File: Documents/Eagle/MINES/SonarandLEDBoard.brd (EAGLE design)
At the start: 60.6 x 49.5 mm, 21 parts, among them X1 B2B-XH-2, X16 B2B-XH-2, X17 B2B-XH-2, X18 B2B-XH-2, X19 B2B-XH-2, X2 B2B-XH-2, X20 B2B-XH-2, X21 B2B-XH-2, X3 B4B-XH-2, X4 B4B-XH-2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

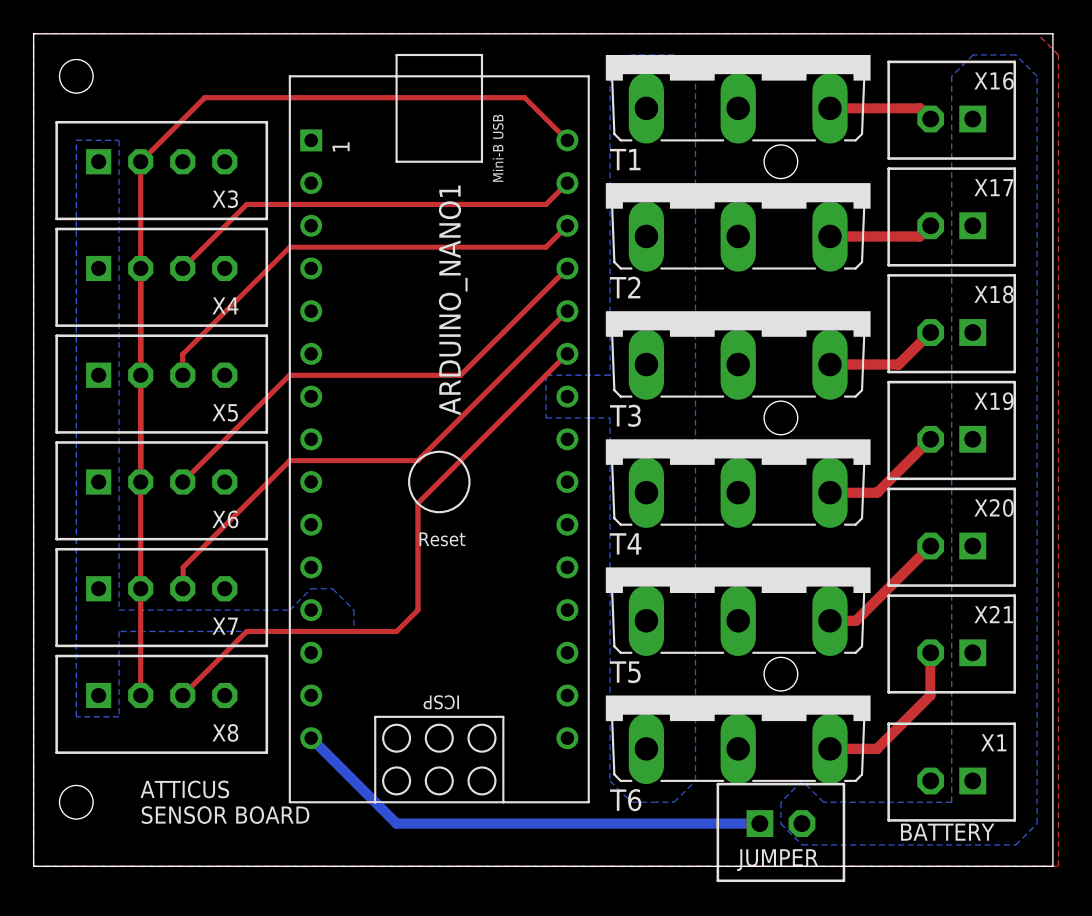
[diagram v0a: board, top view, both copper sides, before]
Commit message: Added 3-head breakouts to both boards and team name
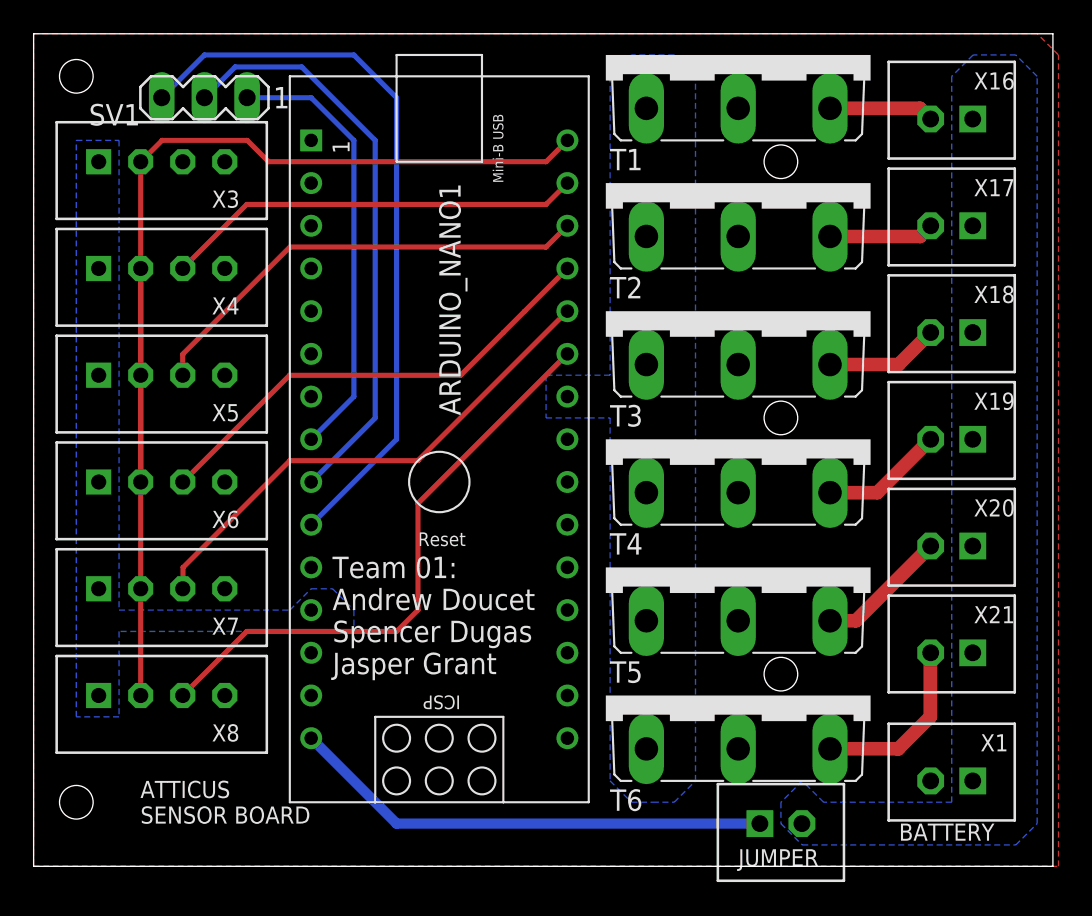
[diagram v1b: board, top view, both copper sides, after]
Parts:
- added SV1: (no value), con-lstb:MA03-1
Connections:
- new net N$1: ARDUINO_NANO1.8, SV1.1
- new net N$3: ARDUINO_NANO1.9, SV1.2
- new net N$4: ARDUINO_NANO1.10, SV1.3
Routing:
- net N$4: track 0.00 -> 43.6 mm
- net N$3: track 0.00 -> 34.6 mm
- net N$1: track 0.00 -> 26.2 mm
- net N$34: track 72.5 -> 71.4 mm
- net N$38: track 9.83 -> 10.6 mm
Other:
- board text added: "Team 01: Andrew Doucet Spencer Dugas Jasper Grant"
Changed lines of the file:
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@@
 <hole x="43.18" y="41.91" drill="2"/>
 <hole x="43.18" y="57.15" drill="2"/>
+<text x="16.51" y="41.91" size="1.27" layer="25">Team 01:
+Andrew Doucet
+Spencer Dugas
+Jasper Grant</text>
 </plain>
 <attributes>
@@
 </element>
 <element name="X2" library="con-JST XH" library_urn="urn:adsk.eagle:library:29976298" package="B2B-XH-A" package3d_urn="urn:adsk.eagle:package:29976402/1" value="B2B-XH-2" x="43.18" y="33.02" smashed="yes" rot="R180"/>
+<element name="SV1" library="con-lstb" library_urn="urn:adsk.eagle:library:162" package="MA03-1" package3d_urn="urn:adsk.eagle:package:8339/1" value="" x="8.89" y="76.2" smashed="yes" rot="R180">
+<attribute name="MF" value="" x="8.89" y="76.2" size="1.778" layer="27" rot="R180" display="off"/>
+<attribute name="MPN" value="" x="8.89" y="76.2" size="1.778" layer="27" rot="R180" display="off"/>
+<attribute name="NAME" x="5.08" y="75.819" size="1.27" layer="25" ratio="10" rot="R180"/>
+<attribute name="OC_FARNELL" value="unknown" x="8.89" y="76.2" size="1.778" layer="27" rot="R180" display="off"/>
+<attribute name="OC_NEWARK" value="unknown" x="8.89" y="76.2" size="1.778" layer="27" rot="R180" display="off"/>
+<attribute name="POPULARITY" value="48" x="8.89" y="76.2" size="1.778" layer="27" rot="R180" display="off"/>
+<attribute name="VALUE" x="12.7" y="79.121" size="1.27" layer="27" ratio="10" rot="R180"/>
+</element>
 </elements>
 <signals>
@@
 <wire x1="5.1" y1="59.69" x2="5.1" y2="66.04" width="0.3048" layer="1"/>
 <contactref element="ARDUINO_NANO1" pad="30"/>
-<wire x1="30.48" y1="73.66" x2="27.94" y2="76.2" width="0.3048" layer="1"/>
-<wire x1="8.91" y1="76.2" x2="5.1" y2="72.39" width="0.3048" layer="1"/>
-<wire x1="27.94" y1="76.2" x2="8.91" y2="76.2" width="0.3048" layer="1"/>
 <wire x1="5.1" y1="40.64" x2="5.1" y2="46.99" width="0.3048" layer="1"/>
+<wire x1="30.48" y1="73.66" x2="29.21" y2="72.39" width="0.3048" layer="1"/>
+<wire x1="29.21" y1="72.39" x2="12.7" y2="72.39" width="0.3048" layer="1"/>
+<wire x1="12.7" y1="72.39" x2="11.43" y2="73.66" width="0.3048" layer="1"/>
+<wire x1="11.43" y1="73.66" x2="6.37" y2="73.66" width="0.3048" layer="1"/>
+<wire x1="6.37" y1="73.66" x2="5.1" y2="72.39" width="0.3048" layer="1"/>
 </signal>
 <signal name="N$35">
@@
 <contactref element="X16" pad="2"/>
 <contactref element="T1" pad="E"/>
-<wire x1="46.101" y1="75.565" x2="51.455" y2="75.565" width="0.6096" layer="1"/>
-<wire x1="51.455" y1="75.565" x2="52.09" y2="74.93" width="0.6096" layer="1"/>
+<wire x1="46.101" y1="75.565" x2="51.455" y2="75.565" width="0.8128" layer="1"/>
+<wire x1="51.455" y1="75.565" x2="52.09" y2="74.93" width="0.8128" layer="1"/>
 </signal>
 <signal name="N$30">
 <contactref element="X17" pad="2"/>
 <contactref element="T2" pad="E"/>
-<wire x1="46.101" y1="67.945" x2="51.455" y2="67.945" width="0.6096" layer="1"/>
-<wire x1="51.455" y1="67.945" x2="52.09" y2="68.58" width="0.6096" layer="1"/>
+<wire x1="46.101" y1="67.945" x2="51.455" y2="67.945" width="0.8128" layer="1"/>
+<wire x1="51.455" y1="67.945" x2="52.09" y2="68.58" width="0.8128" layer="1"/>
 </signal>
 <signal name="N$32">
 <contactref element="X18" pad="2"/>
 <contactref element="T3" pad="E"/>
-<wire x1="46.101" y1="60.325" x2="50.185" y2="60.325" width="0.6096" layer="1"/>
-<wire x1="50.185" y1="60.325" x2="52.09" y2="62.23" width="0.6096" layer="1"/>
+<wire x1="46.101" y1="60.325" x2="50.185" y2="60.325" width="0.8128" layer="1"/>
+<wire x1="50.185" y1="60.325" x2="52.09" y2="62.23" width="0.8128" layer="1"/>
 </signal>
 <signal name="N$33">
 <contactref element="X19" pad="2"/>
 <contactref element="T4" pad="E"/>
-<wire x1="46.101" y1="52.705" x2="48.915" y2="52.705" width="0.6096" layer="1"/>
-<wire x1="48.915" y1="52.705" x2="52.09" y2="55.88" width="0.6096" layer="1"/>
+<wire x1="46.101" y1="52.705" x2="48.915" y2="52.705" width="0.8128" layer="1"/>
+<wire x1="48.915" y1="52.705" x2="52.09" y2="55.88" width="0.8128" layer="1"/>
 </signal>
 <signal name="N$36">
 <contactref element="X20" pad="2"/>
 <contactref element="T5" pad="E"/>
-<wire x1="46.101" y1="45.085" x2="47.645" y2="45.085" width="0.6096" layer="1"/>
-<wire x1="47.645" y1="45.085" x2="52.09" y2="49.53" width="0.6096" layer="1"/>
+<wire x1="46.101" y1="45.085" x2="47.645" y2="45.085" width="0.8128" layer="1"/>
+<wire x1="47.645" y1="45.085" x2="52.09" y2="49.53" width="0.8128" layer="1"/>
 </signal>
 <signal name="N$38">
 <contactref element="X21" pad="2"/>
 <contactref element="T6" pad="E"/>
-<wire x1="52.09" y1="43.18" x2="52.07" y2="43.16" width="0.6096" layer="1"/>
-<wire x1="52.07" y1="43.16" x2="52.07" y2="40.64" width="0.6096" layer="1"/>
-<wire x1="52.07" y1="40.64" x2="48.895" y2="37.465" width="0.6096" layer="1"/>
-<wire x1="48.895" y1="37.465" x2="46.101" y2="37.465" width="0.6096" layer="1"/>
+<wire x1="52.09" y1="43.18" x2="52.07" y2="43.16" width="0.8128" layer="1"/>
+<wire x1="52.07" y1="43.16" x2="52.07" y2="39.37" width="0.8128" layer="1"/>
+<wire x1="52.07" y1="39.37" x2="50.165" y2="37.465" width="0.8128" layer="1"/>
+<wire x1="50.165" y1="37.465" x2="46.101" y2="37.465" width="0.8128" layer="1"/>
 </signal>
 <signal name="N$2">
@@
 <wire x1="20.32" y1="33.02" x2="41.93" y2="33.02" width="0.6096" layer="16"/>
 </signal>
+<signal name="N$1">
+<contactref element="ARDUINO_NANO1" pad="8"/>
+<contactref element="SV1" pad="1"/>
+<wire x1="15.24" y1="55.88" x2="17.78" y2="58.42" width="0.3048" layer="16"/>
+<wire x1="17.78" y1="58.42" x2="17.78" y2="73.66" width="0.3048" layer="16"/>
+<wire x1="17.78" y1="73.66" x2="15.24" y2="76.2" width="0.3048" layer="16"/>
+<wire x1="15.24" y1="76.2" x2="11.43" y2="76.2" width="0.3048" layer="16"/>
+</signal>
+<signal name="N$3">
+<contactref element="ARDUINO_NANO1" pad="9"/>
+<contactref element="SV1" pad="2"/>
+<wire x1="15.24" y1="53.34" x2="19.05" y2="57.15" width="0.3048" layer="16"/>
+<wire x1="19.05" y1="57.15" x2="19.05" y2="73.66" width="0.3048" layer="16"/>
+<wire x1="14.6812" y1="78.0288" x2="10.7188" y2="78.0288" width="0.3048" layer="16"/>
+<wire x1="10.7188" y1="78.0288" x2="8.89" y2="76.2" width="0.3048" layer="16"/>
+<wire x1="19.05" y1="73.66" x2="14.6812" y2="78.0288" width="0.3048" layer="16"/>
+</signal>
+<signal name="N$4">
+<contactref element="ARDUINO_NANO1" pad="10"/>
+<contactref element="SV1" pad="3"/>
+<wire x1="6.35" y1="76.2" x2="8.89" y2="78.74" width="0.3048" layer="16"/>
+<wire x1="8.89" y1="78.74" x2="17.78" y2="78.74" width="0.3048" layer="16"/>
+<wire x1="17.78" y1="78.74" x2="20.32" y2="76.2" width="0.3048" layer="16"/>
+<wire x1="20.32" y1="55.88" x2="15.24" y2="50.8" width="0.3048" layer="16"/>
+<wire x1="20.32" y1="76.2" x2="20.32" y2="55.88" width="0.3048" layer="16"/>
+</signal>
 </signals>
